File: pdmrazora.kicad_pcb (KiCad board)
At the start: 2 copper layers, 109 x 98 mm, 54 parts, among them J1 6473418-1, J2 M6_VBAT, J3 M6_GND, M1000 Module:mega-mcu144/0.7, U1 BTS50010-1TAD, U11 BTS7004-1EPP, U12 BTS7004-1EPP, U13 BTS7004-1EPP, U14 BTS7004-1EPP, U15 BTS7004-1EPP, U16 BTS7004-1EPP, U17 BTS7004-1EPP, U18 BTS7004-1EPP, U2 BTS50010-1TAD, U3 BTS50010-1TAD, U4 BTS50010-1TAD

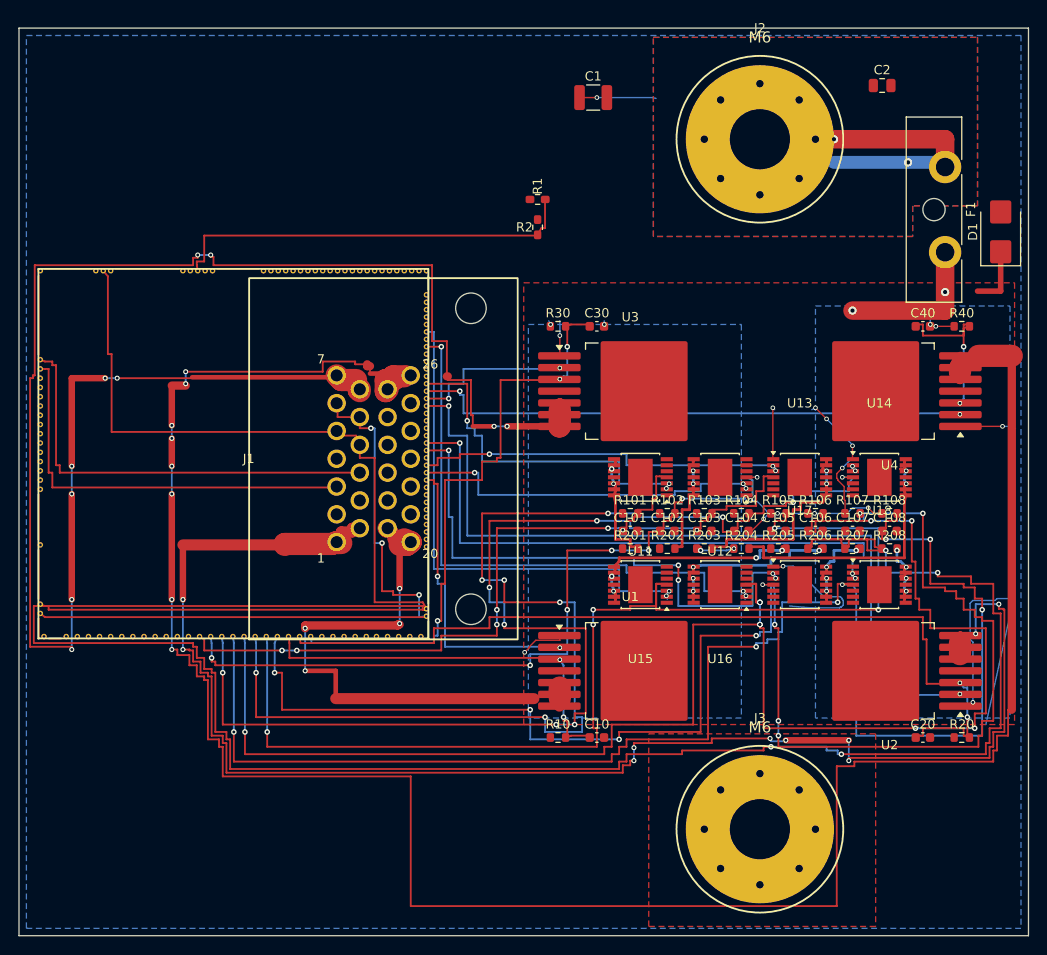
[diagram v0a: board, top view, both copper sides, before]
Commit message: Open SuperSeal exits and stitch carrier GND on the 109×98 board (#16)
* Open SuperSeal exits and stitch carrier GND on the 109x98 board.

Move the SENSOR_GND spine off x=38.40 onto a west bypass so ADIO2/4/6/8
can leave J1, and tie the pour-reachable carrier pads. Unconnected 64 to 53.
F1 stays open, the keepout stays empty, and the 358 HP mask openings are unchanged.

Co-authored-by: Quintin <quintinbannink42@users.noreply.github.com>

* Stitch C2 and C108 onto the GND pour.

Both ties land in the existing B.Cu pour. Unconnected 53 to 51, VBAT stays 10, and the fuse, keepout, and 358 mask openings are unchanged.

Co-authored-by: Quintin <quintinbannink42@users.noreply.github.com>

---------

Co-authored-by: Cursor Agent <cursoragent@cursor.com>
Co-authored-by: Quintin <quintinbannink42@users.noreply.github.com>
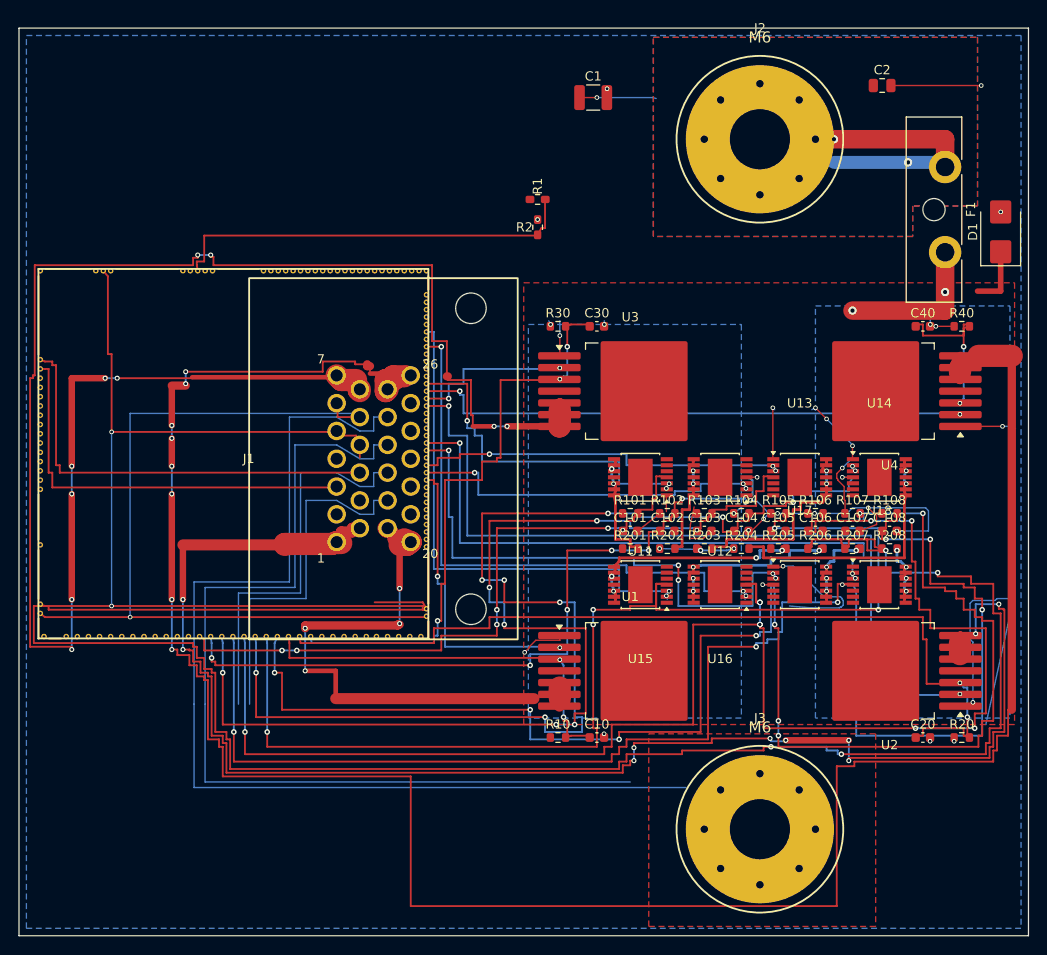
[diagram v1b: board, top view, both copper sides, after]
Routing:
- net ADIO8: track 8.82 -> 124.7 mm
- net ADIO6: track 21.6 -> 125.5 mm
- net ADIO4: track 31.1 -> 74.1 mm
- net ADIO2: track 13.1 -> 51.9 mm
- net GND: track 108.7 -> 146.8 mm, vias 19 -> 29
- net SENSOR_GND: track 74.7 -> 92.4 mm, vias 3 -> 1
- net SENSOR_5V: track 342.1 -> 348.1 mm, vias 6 -> 9
